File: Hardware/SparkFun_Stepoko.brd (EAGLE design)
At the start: 150 x 82 mm, 180 parts, among them J1 AVR ISP, Q1 16MHZ, Q2 100A/100V, U1 ATMEGA328, U2 CY7C65213, U3 74LVC1G04, U4 LM25011, U5 DRV8811, U6 74HC7014D, U7 7432SE, U8 DRV8811, U9 DRV8811

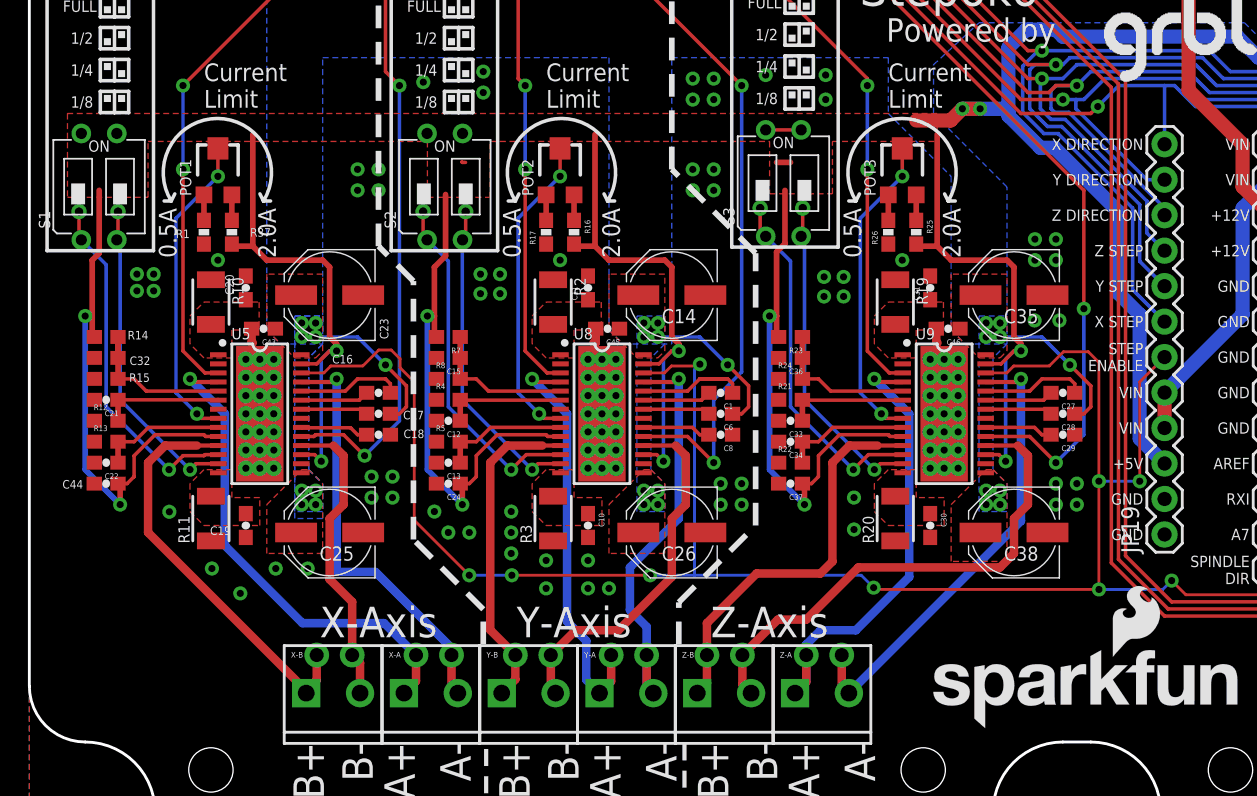
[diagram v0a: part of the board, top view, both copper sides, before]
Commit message: enlarged stepper traces and improved Ground Planes
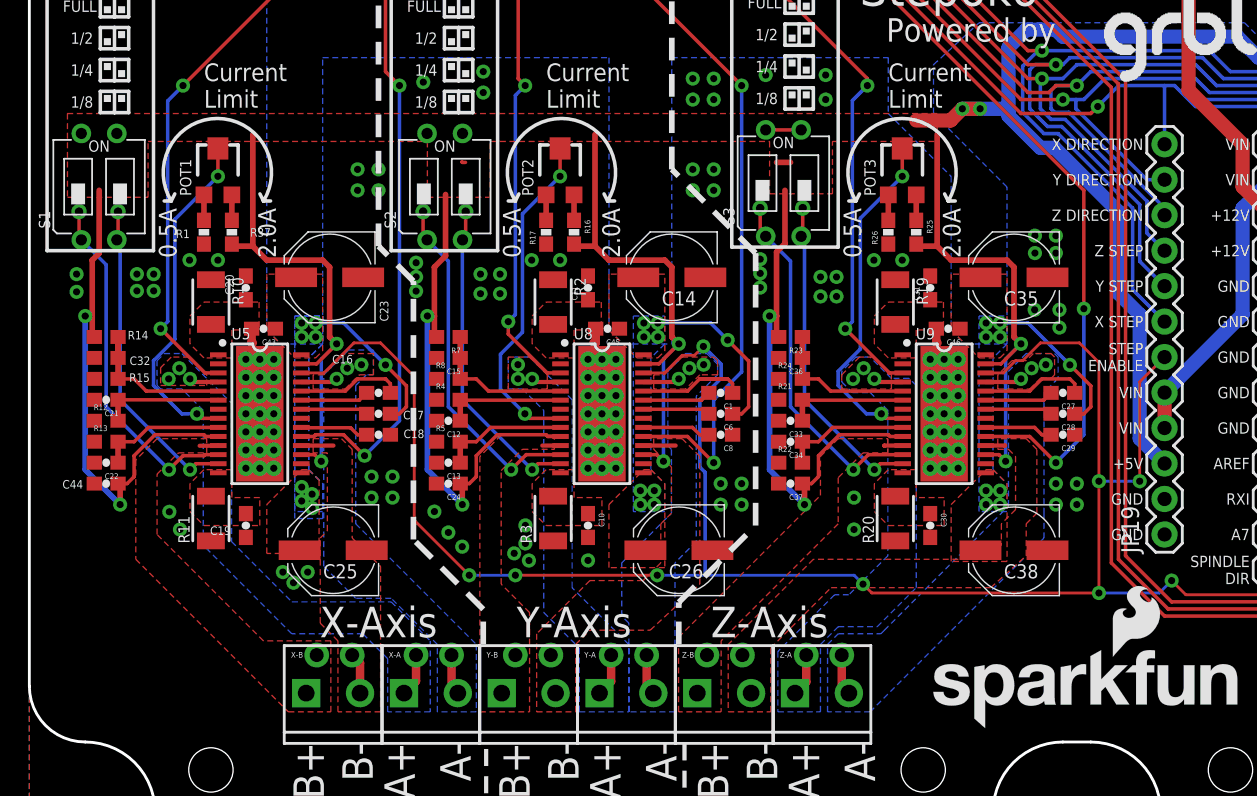
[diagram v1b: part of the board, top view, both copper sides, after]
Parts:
- moved C26 1.37 mm to (46.5, 21.7)
- moved C25 1.30 mm to (21.8, 21.7)
- moved C14 1.27 mm to (46.0, 41.3)
- moved C23 1.27 mm to (21.5, 41.3)
- moved C35 1.27 mm to (70.5, 41.3)
- moved C38 1.27 mm to (70.5, 21.7)
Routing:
- net N$88: track 36.2 -> 1.39 mm
- net N$71: track 35.1 -> 5.20 mm, vias 2 -> 4
- net N$37: track 29.6 -> 1.34 mm
- net N$90: track 33.2 -> 5.56 mm, vias 2 -> 4
- net N$89: track 33.6 -> 6.32 mm, vias 2 -> 4
- net N$87: track 28.7 -> 2.31 mm
- net N$56: track 29.7 -> 5.19 mm, vias 2 -> 4
- net N$79: track 30.3 -> 6.04 mm, vias 2 -> 4
- net N$58: track 30.2 -> 6.23 mm, vias 2 -> 4
- net N$55: track 26.3 -> 2.80 mm
- net N$50: track 23.2 -> 1.30 mm
- net N$69: track 21.6 -> 5.26 mm
- net STEP_ENABLE: track 171.0 -> 175.5 mm
- net VIN: track 81.6 -> 83.9 mm
- net N$94: track 22.5 -> 24.5 mm
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- added copper zone on layer 1, net N$37
- added copper zone on layer 1, net N$50
- added copper zone on layer 1, net N$55
- added copper zone on layer 1, net N$56
- added copper zone on layer 16, net N$56
- added copper zone on layer 1, net N$58
- added copper zone on layer 16, net N$58
- added copper zone on layer 1, net N$69
- added copper zone on layer 1, net N$71
- added copper zone on layer 16, net N$71
- added copper zone on layer 1, net N$79
- added copper zone on layer 16, net N$79
- added copper zone on layer 1, net N$87
- added copper zone on layer 1, net N$88
- added copper zone on layer 1, net N$89
- added copper zone on layer 16, net N$89
- added copper zone on layer 1, net N$90
- added copper zone on layer 16, net N$90

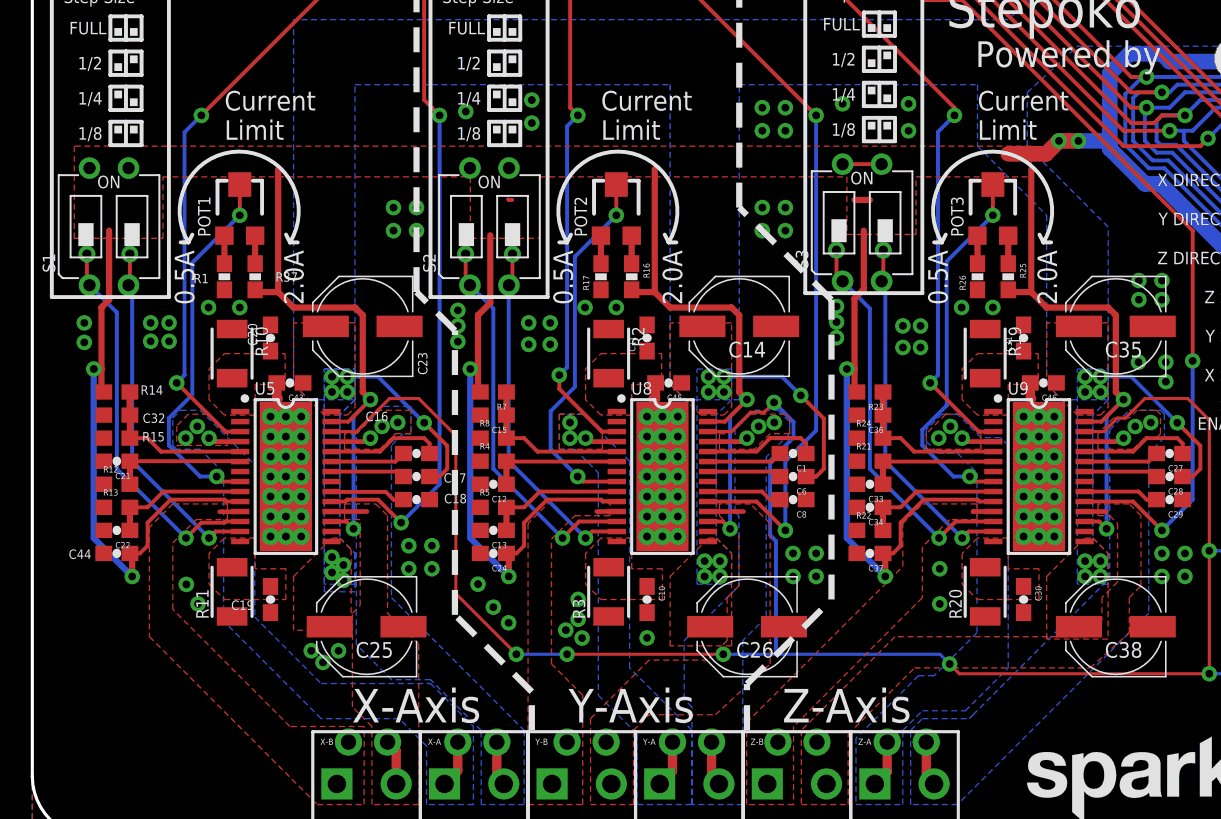
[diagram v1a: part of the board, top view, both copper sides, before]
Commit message: moving components for ground pours
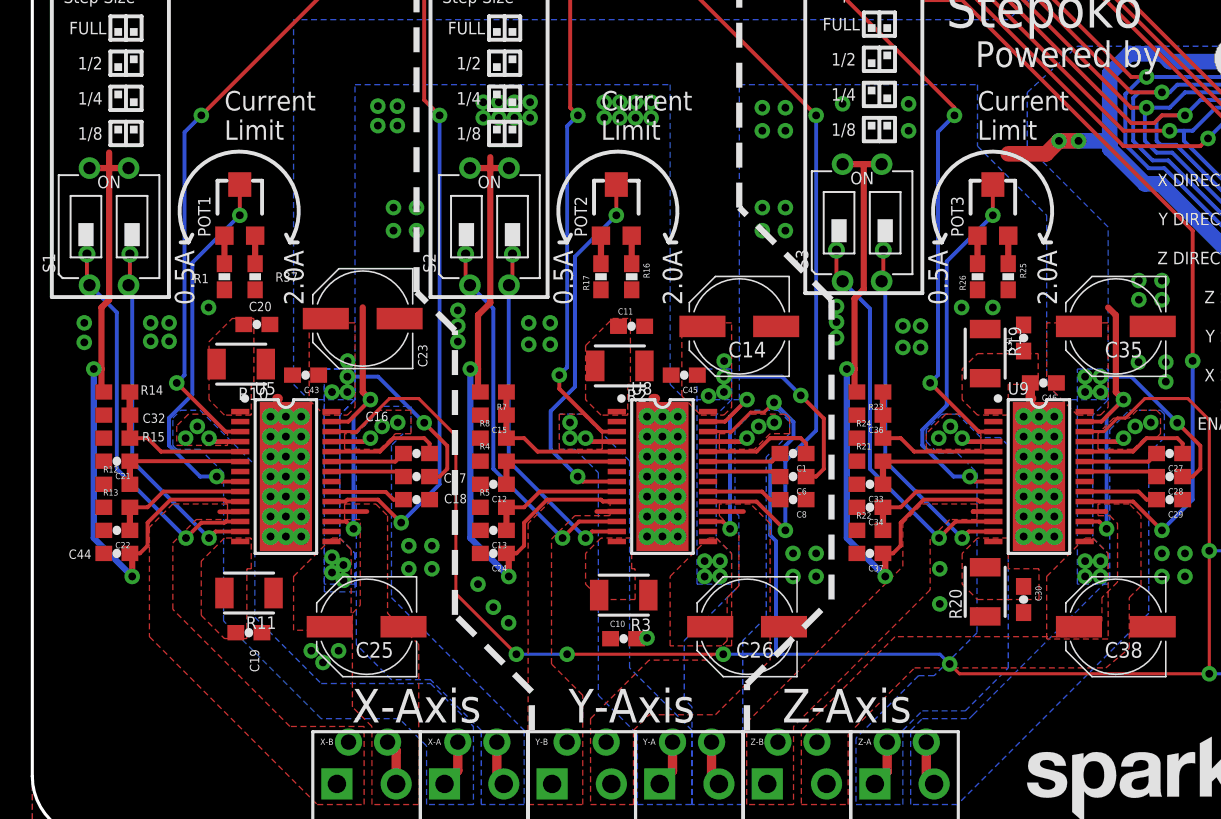
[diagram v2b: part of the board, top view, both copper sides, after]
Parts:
- moved C10 2.97 mm to (38.5, 20.9), turned to 0 degrees
- moved C19 2.58 mm to (14.1, 21.3), turned to 0 degrees
- moved C11 1.26 mm to (39.0, 41.3), turned to 0 degrees
- moved C20 1.25 mm to (14.6, 41.4), turned to 0 degrees
- moved C43 1.14 mm to (17.8, 38.1)
- moved C45 1.14 mm to (42.4, 38.1)
- moved R11 1.10 mm to (14.1, 23.9), turned to 180 degrees
- moved R2 1.08 mm to (38.2, 38.7), turned to 180 degrees
- moved R3 1.01 mm to (38.5, 23.8), turned to 180 degrees
- moved R10 0.90 mm to (13.6, 38.8), turned to 180 degrees
- moved C23 0.51 mm to (21.5, 41.8)
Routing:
- net 5V: track 473.9 -> 440.9 mm
- net GND: track 8.32 -> 6.29 mm, vias 140 -> 148

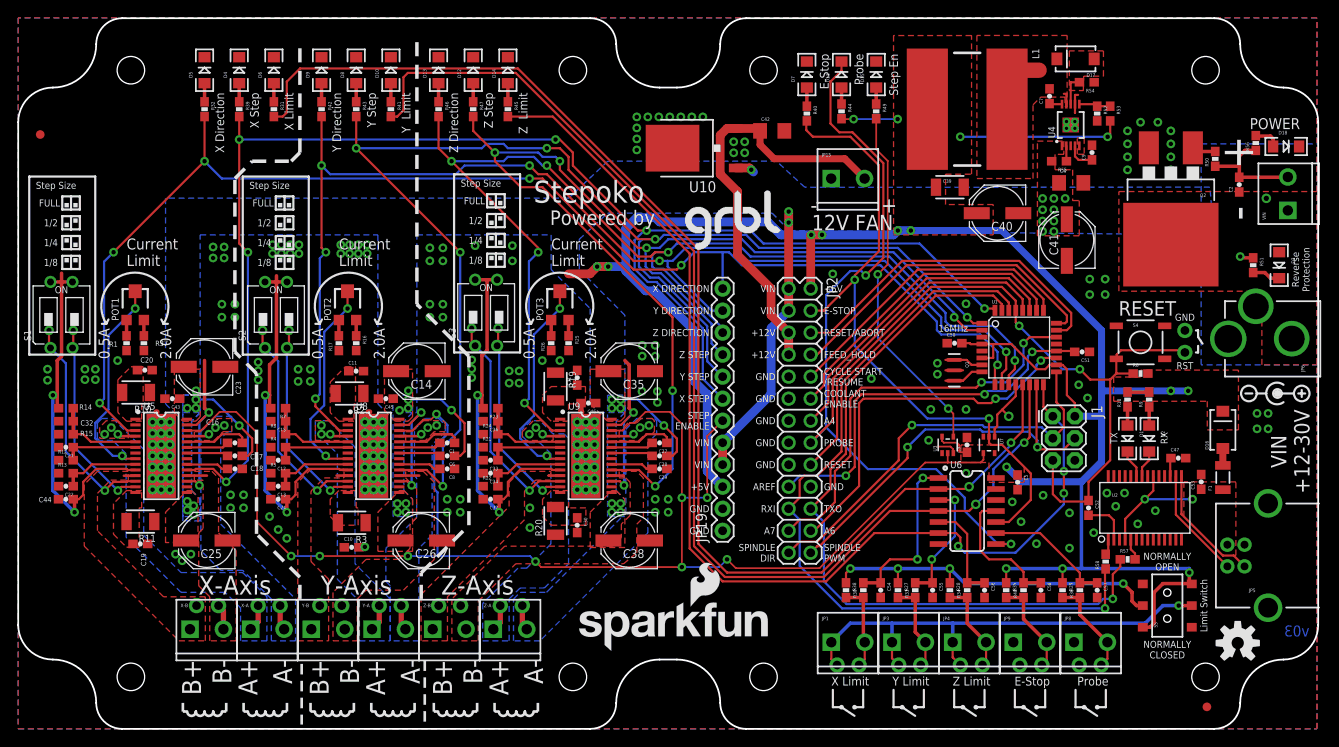
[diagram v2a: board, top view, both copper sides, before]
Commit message: more work on power planes
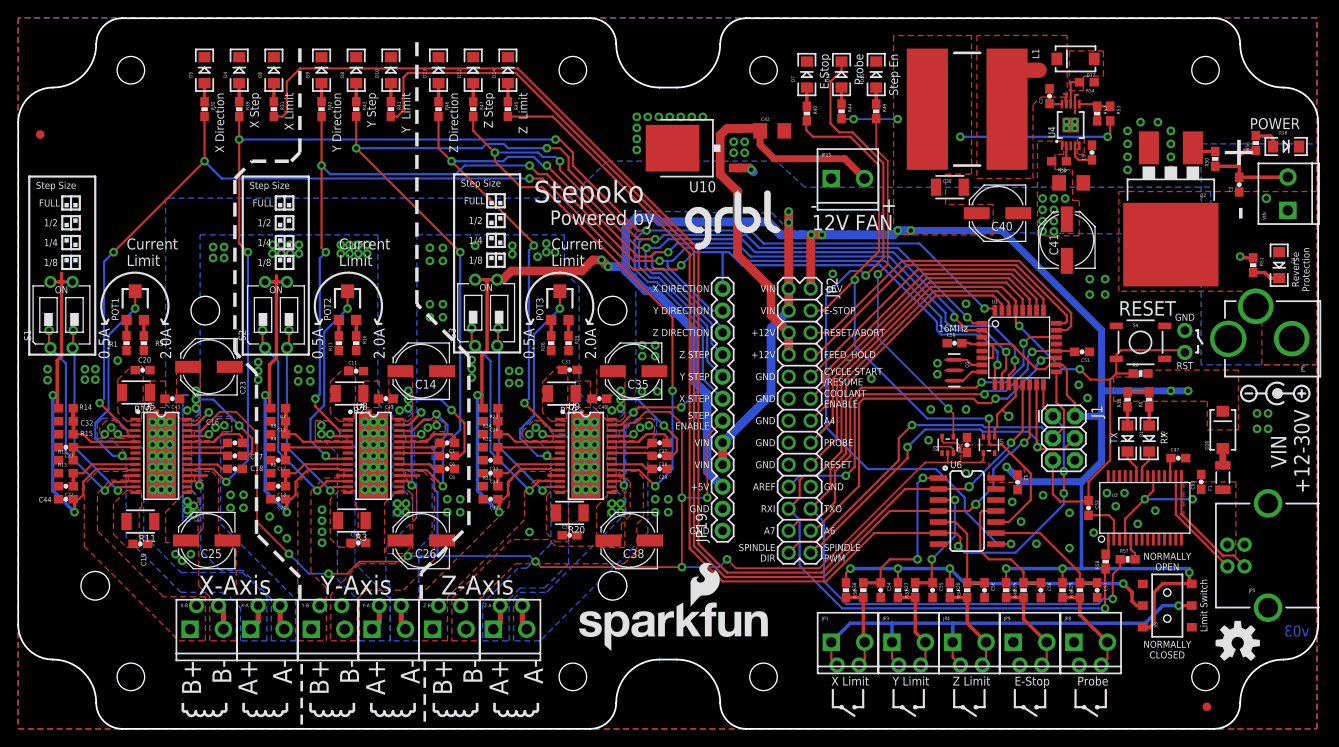
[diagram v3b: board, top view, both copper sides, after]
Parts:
- added U$2, U$3, U$4, U$5: (no value), SparkFun-Electromechanical:STAND-OFF
- moved LOGO3 2.54 mm to (89.9, 8.89)
- moved R20 1.87 mm to (63.6, 24.9), turned to 180 degrees
- moved C30 1.46 mm to (63.6, 22.3), turned to 0 degrees
- moved C46 1.37 mm to (67.1, 38.1)
- moved C31 1.25 mm to (63.6, 41.4), turned to 0 degrees
- moved R19 1.08 mm to (62.7, 38.7), turned to 180 degrees
- moved C10 0.92 mm to (39.2, 21.5)
- moved C14 0.51 mm to (46.5, 41.3)
- moved C23 0.51 mm to (22.0, 41.8)
- moved C35 0.51 mm to (71.0, 41.3)
- moved C20 0.25 mm to (14.4, 41.4)
- moved R3 0.25 mm to (38.5, 24.0)
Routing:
- net 5V: track 440.9 -> 446.3 mm, vias 28 -> 29
- net STEP_ENABLE: track 175.5 -> 177.2 mm
- net GND: track 6.29 -> 5.27 mm, vias 148 -> 147

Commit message: Testing Assembly Variants
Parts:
- moved U$3 1.27 mm to (68.6, 15.2)
- moved U$5 1.27 mm to (8.89, 15.2)
- moved LOGO2 1.27 mm to (64.0, 7.62)
- moved LOGO3 1.27 mm to (89.9, 7.62)
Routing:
- net 5V: track 446.3 -> 615.3 mm, vias 29 -> 41
- net D4-STEP-Z: track 143.4 -> 120.0 mm, vias 6 -> 7
- net D10-LIM-Y: track 136.0 -> 130.0 mm, vias 2 -> 4
- net D3-STEP-Y: track 158.6 -> 153.5 mm, vias 6 -> 7
- net D9-LIM-X: track 147.1 -> 142.3 mm, vias 2 -> 4
- net D5-DIR-X: track 154.5 -> 157.2 mm
- net D2-STEP-X: track 170.0 -> 171.7 mm
- net VIN: track 83.9 -> 82.9 mm, vias 40 -> 39
- net D7-DIR-Z: track 139.1 -> 138.1 mm, vias 6 -> 7
- net GND: vias 147 -> 149

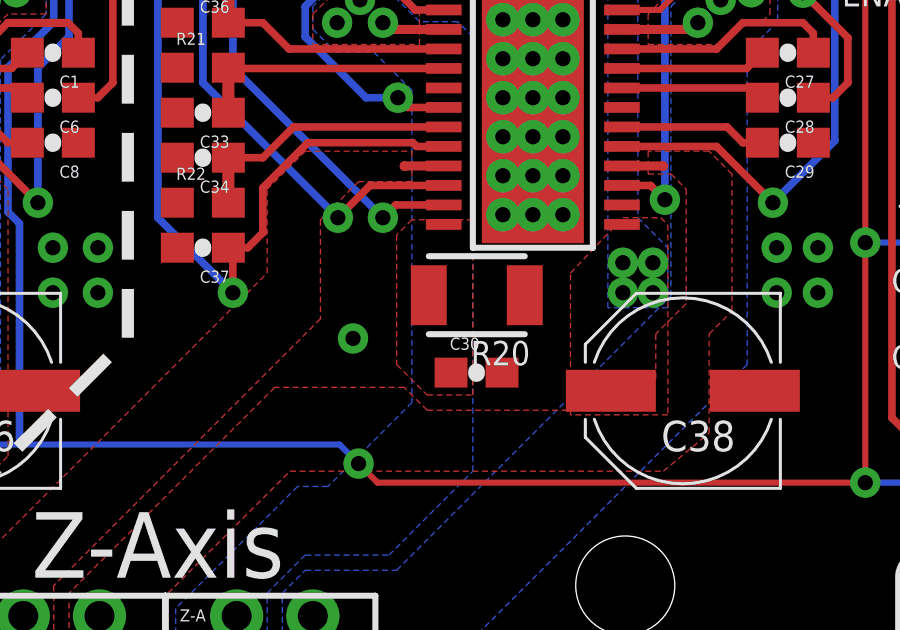
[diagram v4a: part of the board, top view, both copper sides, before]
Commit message: adding room for heatsinks
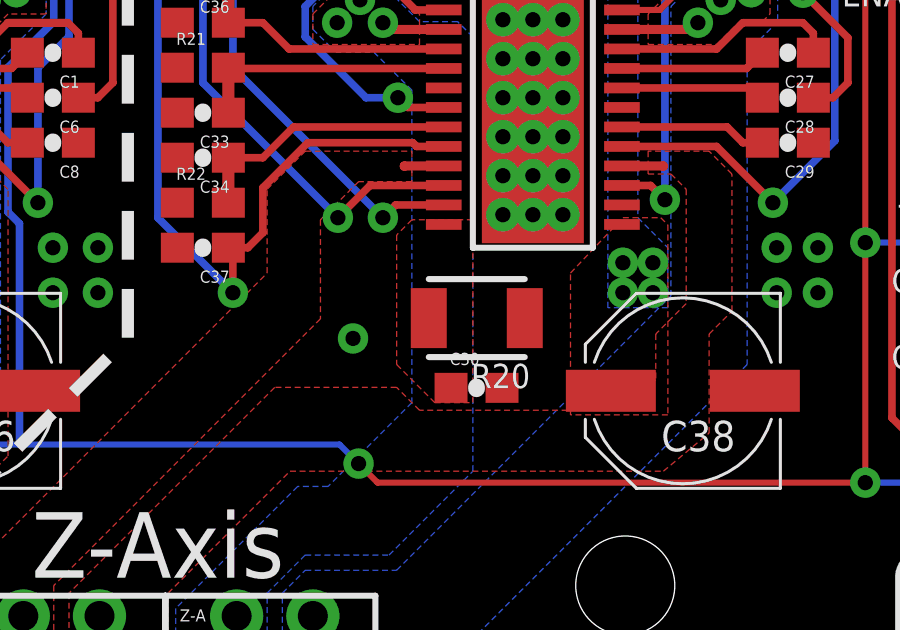
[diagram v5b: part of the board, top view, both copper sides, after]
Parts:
- moved R20 0.76 mm to (63.6, 24.2)
- moved C30 0.51 mm to (63.6, 21.8)
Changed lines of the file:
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@@
 <setting verticaltext="up"/>
 </settings>
-<grid distance="0.005" unitdist="inch" unit="inch" style="lines" multiple="1" display="yes" altdistance="0.01" altunitdist="mm" altunit="mm"/>
+<grid distance="0.01" unitdist="inch" unit="inch" style="lines" multiple="1" display="yes" altdistance="0.01" altunitdist="mm" altunit="mm"/>
 <layers>
 <layer number="1" name="Top" color="4" fill="1" visible="yes" active="yes"/>
@@
 <text x="87.376" y="20.32" size="0.8128" layer="21" font="vector" ratio="15" align="center-right">SPINDLE
 DIR</text>
+<wire x1="74.93" y1="52.07" x2="74.93" y2="10.16" width="0.4064" layer="49"/>
+<wire x1="74.93" y1="10.16" x2="2.54" y2="10.16" width="0.4064" layer="49"/>
+<wire x1="2.54" y1="10.16" x2="2.54" y2="52.07" width="0.4064" layer="49"/>
+<wire x1="2.54" y1="52.07" x2="74.93" y2="52.07" width="0.4064" layer="49"/>
+<wire x1="12.7" y1="25.4" x2="68.58" y2="25.4" width="0.4064" layer="22"/>
+<wire x1="68.58" y1="25.4" x2="68.58" y2="38.1" width="0.4064" layer="22"/>
+<wire x1="68.58" y1="38.1" x2="12.7" y2="38.1" width="0.4064" layer="22"/>
+<wire x1="12.7" y1="38.1" x2="12.7" y2="25.4" width="0.4064" layer="22"/>
+<wire x1="14.478" y1="26.416" x2="14.478" y2="36.576" width="0.4064" layer="49"/>
+<wire x1="14.478" y1="36.576" x2="67.564" y2="36.576" width="0.4064" layer="49"/>
+<wire x1="67.564" y1="36.576" x2="67.564" y2="26.416" width="0.4064" layer="49"/>
+<wire x1="67.564" y1="26.416" x2="14.478" y2="26.416" width="0.4064" layer="49"/>
 </plain>
 <attributes>
 </attributes>
 <variantdefs>
-<variantdef name="Testing"/>
 </variantdefs>
 <classes>
@@
 <attribute name="PROD_ID" value="CAP-09885" x="81" y="12" size="1.778" layer="27" rot="R180" display="off"/>
 </element>
-<element name="C30" library="SparkFun-Capacitors" package="0603-CAP" value="0.1uF" x="63.622" y="22.336">
-<attribute name="PROD_ID" value="CAP-00810" x="53.122" y="37.336" size="1.778" layer="27" display="off"/>
+<element name="C30" library="SparkFun-Capacitors" package="0603-CAP" value="0.1uF" x="63.622" y="21.828">
+<attribute name="PROD_ID" value="CAP-00810" x="53.122" y="36.828" size="1.778" layer="27" display="off"/>
 </element>
 <element name="C31" library="SparkFun-Capacitors" package="0603-CAP" value="0.1uF" x="63.63" y="41.418">
@@
 <attribute name="PROD_ID" value="RES-12374" x="76.714" y="37.184" size="1.778" layer="27" rot="R180" display="off"/>
 </element>
-<element name="R20" library="SparkFun-Resistors" package="1210" value="0.1" x="63.63" y="24.916" rot="R180">
-<attribute name="PROD_ID" value="RES-12374" x="82.63" y="28.916" size="1.778" layer="27" rot="R180" display="off"/>
+<element name="R20" library="SparkFun-Resistors" package="1210" value="0.1" x="63.63" y="24.154" rot="R180">
+<attribute name="PROD_ID" value="RES-12374" x="82.63" y="28.154" size="1.778" layer="27" rot="R180" display="off"/>
 </element>
 <element name="R21" library="SparkFun-Resistors" package="0603" value="39K" x="54.5" y="32.5">
@@
 <vertex x="69.596" y="22.098"/>
 <vertex x="68.58" y="21.082"/>
-<vertex x="61.976" y="21.082"/>
-<vertex x="61.214" y="21.844"/>
+<vertex x="61.722" y="21.082"/>
+<vertex x="60.96" y="21.844"/>
 <vertex x="56.896" y="21.844"/>
 <vertex x="50.038" y="14.986"/>
@@
 <vertex x="60.96" y="26.924"/>
 <vertex x="60.96" y="22.606"/>
-<vertex x="61.976" y="21.59"/>
-<vertex x="63.5" y="21.59"/>
+<vertex x="62.23" y="21.336"/>
+<vertex x="63.5" y="21.336"/>
 </polygon>
 </signal>

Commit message: updated version numbers
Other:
- board text added: "v04"
- board text removed: "v03"
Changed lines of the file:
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@@
 <board>
 <plain>
-<text x="148.99" y="10.66" size="1.27" layer="16" font="vector" ratio="20" rot="MR0">v03</text>
+<text x="148.99" y="10.66" size="1.27" layer="16" font="vector" ratio="20" rot="MR0">v04</text>
 <text x="149" y="32" size="1.778" layer="21" font="vector" ratio="15" rot="R90" align="bottom-center">VIN
 +12-30V</text>
